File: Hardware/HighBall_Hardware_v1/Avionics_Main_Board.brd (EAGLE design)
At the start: 171.4 x 88.9 mm, 21 parts

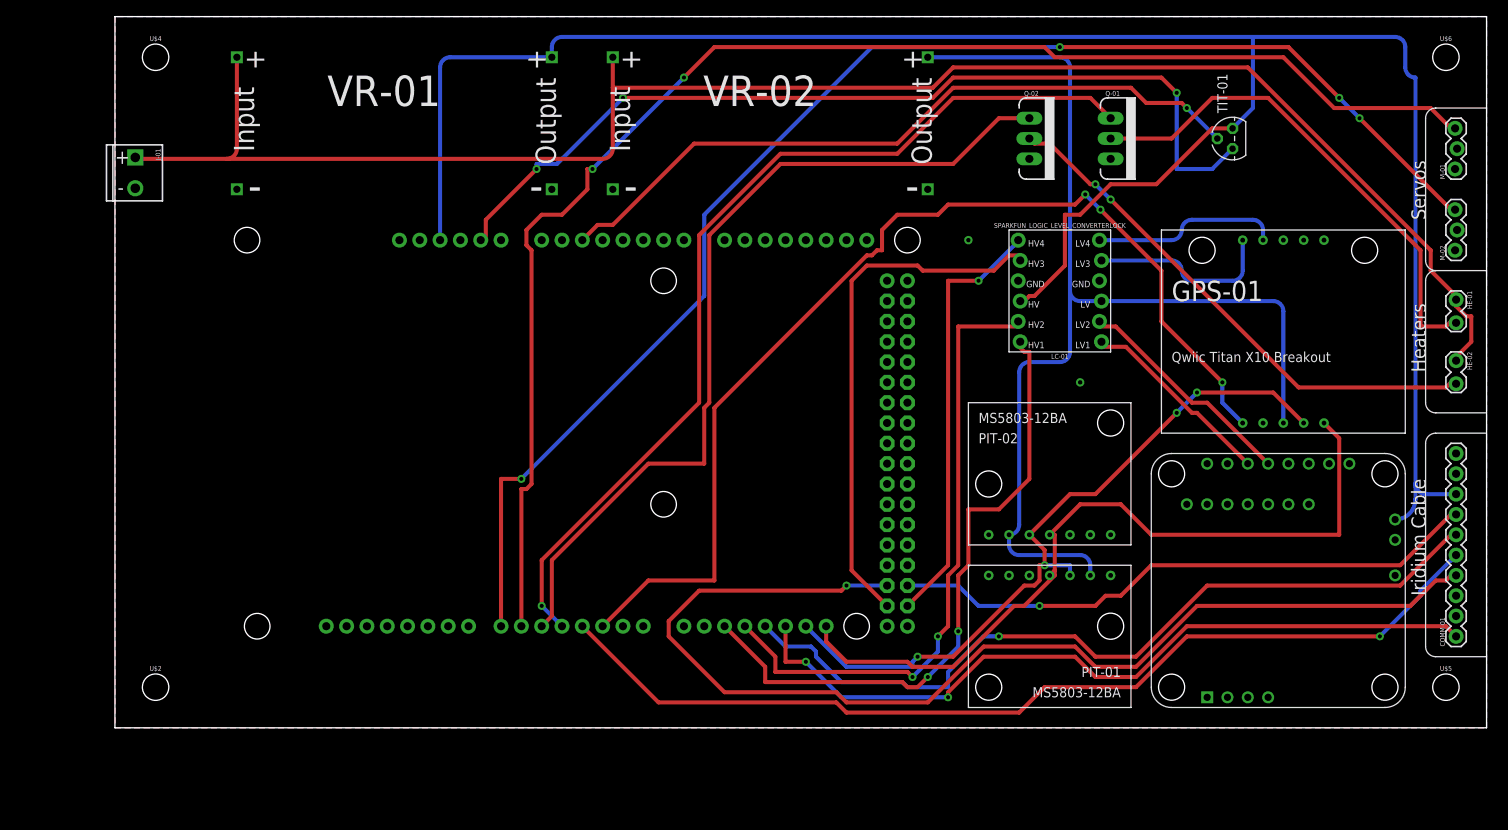
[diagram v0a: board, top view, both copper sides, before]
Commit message: Code and Schematic Updates
Added State Machine .h & .cpp file
Added Resistor to LM335 and added battery voltage measurement to schematic.
Board Layout TBD
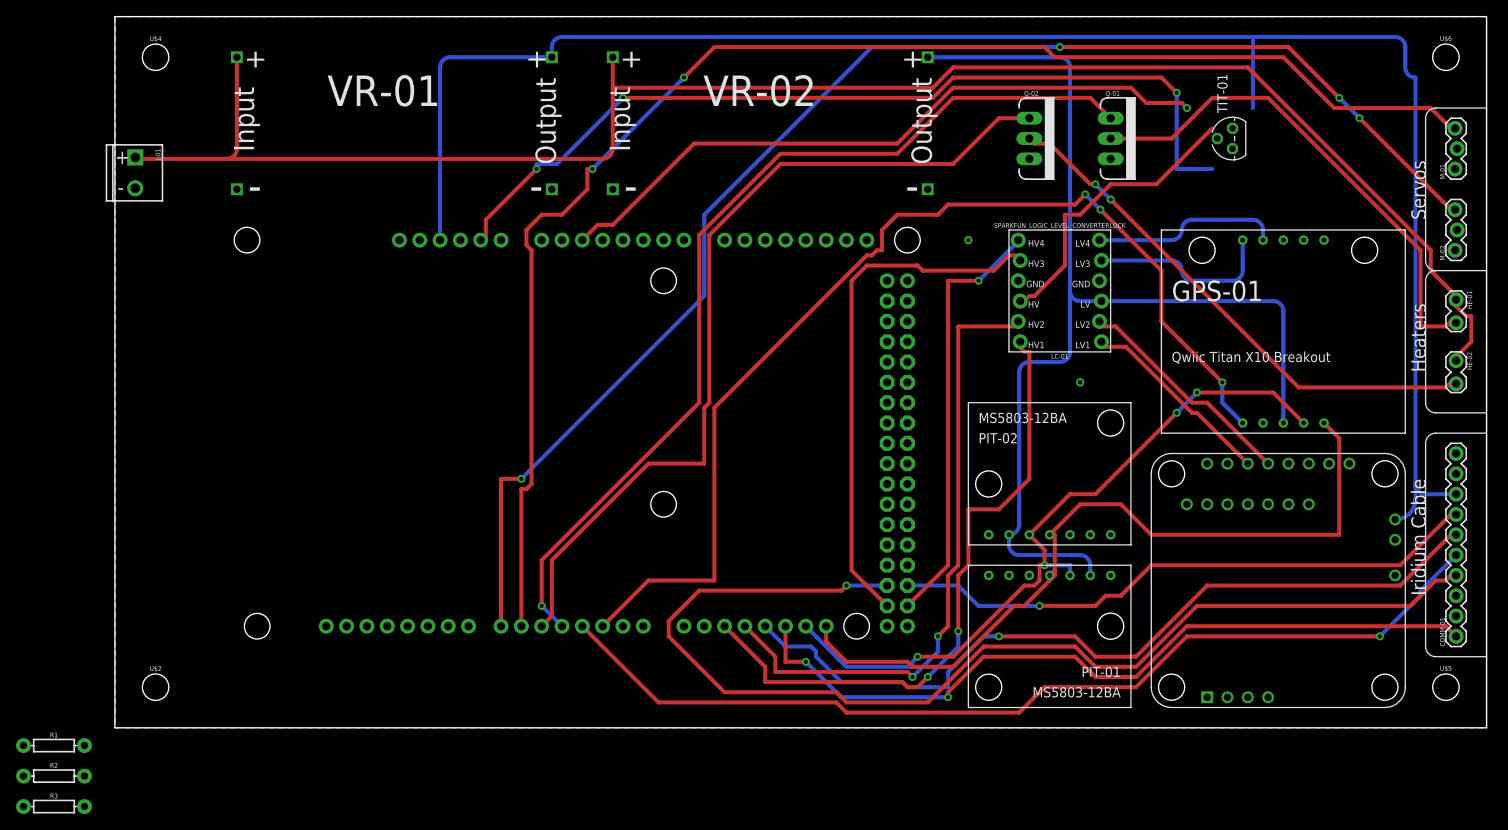
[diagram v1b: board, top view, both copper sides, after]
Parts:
- added R1: 2k, SparkFun-Resistors:AXIAL-0.3
- added R2: 20k, SparkFun-Resistors:AXIAL-0.3
- added R3: 130k, SparkFun-Resistors:AXIAL-0.3
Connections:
- new net VBAT_SENSE: C-1.A3, R2.P$1, R3.P$2
- net AGND: now also TIT-01.1; no longer TIT-01.3
- net GND: now also R3.P$1
- net TIT-01: now also R1.P$2
- net VBAT: now also R2.P$2
- net VCC_1: now also R1.P$1; no longer TIT-01.1
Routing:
- net VCC_1: track 263.0 -> 256.9 mm
- net TIT-01: track 89.9 -> 84.5 mm
- net AGND: track 115.6 -> 112.0 mm
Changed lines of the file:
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@@
 <?xml version="1.0" encoding="utf-8"?>
 <!DOCTYPE eagle SYSTEM "eagle.dtd">
-<eagle version="9.1.1">
+<eagle version="9.1.2">
 <drawing>
 <settings>
-<setting alwaysvectorfont="yes"/>
+<setting alwaysvectorfont="no"/>
 <setting verticaltext="up"/>
 </settings>
@@
 <element name="U$5" library="SparkFun-Hardware" library_urn="urn:adsk.eagle:library:519" package="STAND-OFF" package3d_urn="urn:adsk.eagle:package:38630/1" value="" x="166.37" y="5.08"/>
 <element name="U$6" library="SparkFun-Hardware" library_urn="urn:adsk.eagle:library:519" package="STAND-OFF" package3d_urn="urn:adsk.eagle:package:38630/1" value="" x="166.37" y="83.82"/>
+<element name="R1" library="SparkFun-Resistors" library_urn="urn:adsk.eagle:library:532" package="AXIAL-0.3" package3d_urn="urn:adsk.eagle:package:39658/1" value="2k" x="-7.62" y="-2.2225">
+<attribute name="PROD_ID" value="RES-08380" x="-7.62" y="-2.2225" size="1.778" layer="27" display="off"/>
+</element>
+<element name="R2" library="SparkFun-Resistors" library_urn="urn:adsk.eagle:library:532" package="AXIAL-0.3" package3d_urn="urn:adsk.eagle:package:39658/1" value="20k" x="-7.62" y="-6.0325">
+<attribute name="PROD_ID" value="RES-08380" x="-7.62" y="-6.0325" size="1.778" layer="27" display="off"/>
+</element>
+<element name="R3" library="SparkFun-Resistors" library_urn="urn:adsk.eagle:library:532" package="AXIAL-0.3" package3d_urn="urn:adsk.eagle:package:39658/1" value="130k" x="-7.62" y="-9.8425">
+<attribute name="PROD_ID" value="RES-08380" x="-7.62" y="-9.8425" size="1.778" layer="27" display="off"/>
+</element>
 </elements>
 <signals>
@@
 <wire x1="62.23" y1="80.01" x2="102.235" y2="80.01" width="0.508" layer="1"/>
 <wire x1="167.64" y1="53.975" x2="167.64" y2="53.5178" width="0.508" layer="1"/>
+<contactref element="R2" pad="P$2"/>
+<wire x1="-3.81" y1="-6.0325" x2="2.7178" y2="71.12" width="0" layer="19" extent="1-1"/>
 </signal>
 <signal name="GND">
@@
 <via x="106.68" y="60.96" extent="1-16" drill="0.55"/>
 <via x="120.65" y="43.18" extent="1-16" drill="0.55"/>
+<contactref element="R3" pad="P$1"/>
+<wire x1="160.02" y1="23.495" x2="167.64" y2="34.29" width="0" layer="19" extent="1-1"/>
+<wire x1="143.51" y1="38.1" x2="160.02" y2="23.495" width="0" layer="19" extent="1-1"/>
+<wire x1="120.65" y1="43.18" x2="143.51" y2="38.1" width="0" layer="19" extent="1-1"/>
+<wire x1="123.063" y1="55.88" x2="120.65" y2="43.18" width="0" layer="19" extent="1-1"/>
+<wire x1="112.903" y1="55.88" x2="123.063" y2="55.88" width="0" layer="19" extent="1-1"/>
+<wire x1="106.68" y1="60.96" x2="112.903" y2="55.88" width="0" layer="19" extent="1-1"/>
+<wire x1="101.6" y1="67.31" x2="106.68" y2="60.96" width="0" layer="19" extent="1-1"/>
+<wire x1="114.3" y1="71.12" x2="106.68" y2="60.96" width="0" layer="19" extent="1-1"/>
+<wire x1="124.46" y1="71.12" x2="114.3" y2="71.12" width="0" layer="19" extent="1-1"/>
+<wire x1="109.22" y1="24.13" x2="120.65" y2="43.18" width="0" layer="19" extent="1-1"/>
+<wire x1="124.46" y1="19.05" x2="109.22" y2="24.13" width="0" layer="19" extent="1-1"/>
+<wire x1="62.23" y1="67.31" x2="101.6" y2="67.31" width="0" layer="19" extent="1-1"/>
+<wire x1="54.61" y1="67.31" x2="62.23" y2="67.31" width="0" layer="19" extent="1-1"/>
+<wire x1="43.18" y1="60.96" x2="54.61" y2="67.31" width="0" layer="19" extent="1-1"/>
+<wire x1="15.24" y1="67.31" x2="43.18" y2="60.96" width="0" layer="19" extent="1-1"/>
+<wire x1="2.54" y1="67.4422" x2="15.24" y2="67.31" width="0" layer="19" extent="1-1"/>
+<wire x1="-11.43" y1="-9.8425" x2="2.54" y2="67.4422" width="0" layer="19" extent="1-1"/>
 </signal>
 <signal name="VCC_1">
 <contactref element="VR-01" pad="OUT+"/>
 <contactref element="C-1" pad="5V@0"/>
-<contactref element="TIT-01" pad="1"/>
 <contactref element="IMU-01" pad="VBAT"/>
 <contactref element="LC-01" pad="HV"/>
@@
 <wire x1="160.02" y1="86.36" x2="142.24" y2="86.36" width="0.508" layer="16"/>
 <wire x1="142.24" y1="86.36" x2="55.88" y2="86.36" width="0.508" layer="16"/>
-<wire x1="142.24" y1="77.47" x2="139.7" y2="74.93" width="0.508" layer="16"/>
 <wire x1="142.24" y1="86.36" x2="142.24" y2="77.47" width="0.508" layer="16"/>
 <wire x1="114.3" y1="53.975" x2="113.665" y2="53.34" width="0.508" layer="1"/>
@@
 <wire x1="130.175" y1="67.945" x2="124.46" y2="67.945" width="0.508" layer="1"/>
 <wire x1="137.16" y1="74.93" x2="130.175" y2="67.945" width="0.508" layer="1"/>
-<wire x1="139.7" y1="74.93" x2="137.16" y2="74.93" width="0.508" layer="1"/>
 <wire x1="113.665" y1="53.34" x2="113.157" y2="53.34" width="0.508" layer="1"/>
+<contactref element="R1" pad="P$1"/>
+<wire x1="142.24" y1="77.47" x2="137.16" y2="74.93" width="0" layer="19" extent="1-16"/>
+<wire x1="-11.43" y1="-2.2225" x2="40.64" y2="60.96" width="0" layer="19" extent="1-1"/>
 </signal>
 <signal name="VCC_2">
@@
 <signal name="AGND">
 <contactref element="C-1" pad="GND@1"/>
-<contactref element="TIT-01" pad="3"/>
-<wire x1="137.16" y1="69.85" x2="139.7" y2="72.39" width="0.508" layer="16"/>
 <wire x1="132.715" y1="69.85" x2="137.16" y2="69.85" width="0.508" layer="16"/>
 <wire x1="132.715" y1="79.375" x2="132.715" y2="69.85" width="0.508" layer="16"/>
@@
 <via x="63.5" y="78.74" extent="1-16" drill="0.508"/>
 <via x="52.705" y="69.85" extent="1-16" drill="0.508"/>
+<contactref element="TIT-01" pad="1"/>
+<wire x1="137.16" y1="69.85" x2="139.7" y2="74.93" width="0" layer="19" extent="16-16"/>
 </signal>
 <signal name="TIT-01">
 <contactref element="C-1" pad="A2"/>
-<contactref element="TIT-01" pad="2"/>
-<wire x1="133.985" y1="77.47" x2="137.795" y2="73.66" width="0.508" layer="16"/>
 <wire x1="133.35" y1="78.105" x2="133.985" y2="77.47" width="0.508" layer="1"/>
 <wire x1="128.905" y1="78.105" x2="133.35" y2="78.105" width="0.508" layer="1"/>
@@
 <wire x1="58.42" y1="60.96" x2="60.325" y2="62.865" width="0.508" layer="1"/>
 <via x="133.985" y="77.47" extent="1-16" drill="0.508"/>
+<contactref element="R1" pad="P$2"/>
+<contactref element="TIT-01" pad="2"/>
+<wire x1="133.985" y1="77.47" x2="137.795" y2="73.66" width="0" layer="19" extent="1-1"/>
+<wire x1="-3.81" y1="-2.2225" x2="58.42" y2="60.96" width="0" layer="19" extent="1-1"/>
 </signal>
 <signal name="IMU-01-RX">
@@
 <via x="115.57" y="15.24" extent="1-16" drill="0.508"/>
 </signal>
+<signal name="VBAT_SENSE">
+<contactref element="R2" pad="P$1"/>
+<contactref element="R3" pad="P$2"/>
+<contactref element="C-1" pad="A3"/>
+<wire x1="-3.81" y1="-9.8425" x2="60.96" y2="60.96" width="0" layer="19" extent="1-1"/>
+<wire x1="-11.43" y1="-6.0325" x2="-3.81" y2="-9.8425" width="0" layer="19" extent="1-1"/>
+</signal>
 </signals>

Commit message: Schematic Rev C and CAD Files changes
Completed rev C of hardware schematic
Created new PCB layout
Updated tolerance on ballast dispenser
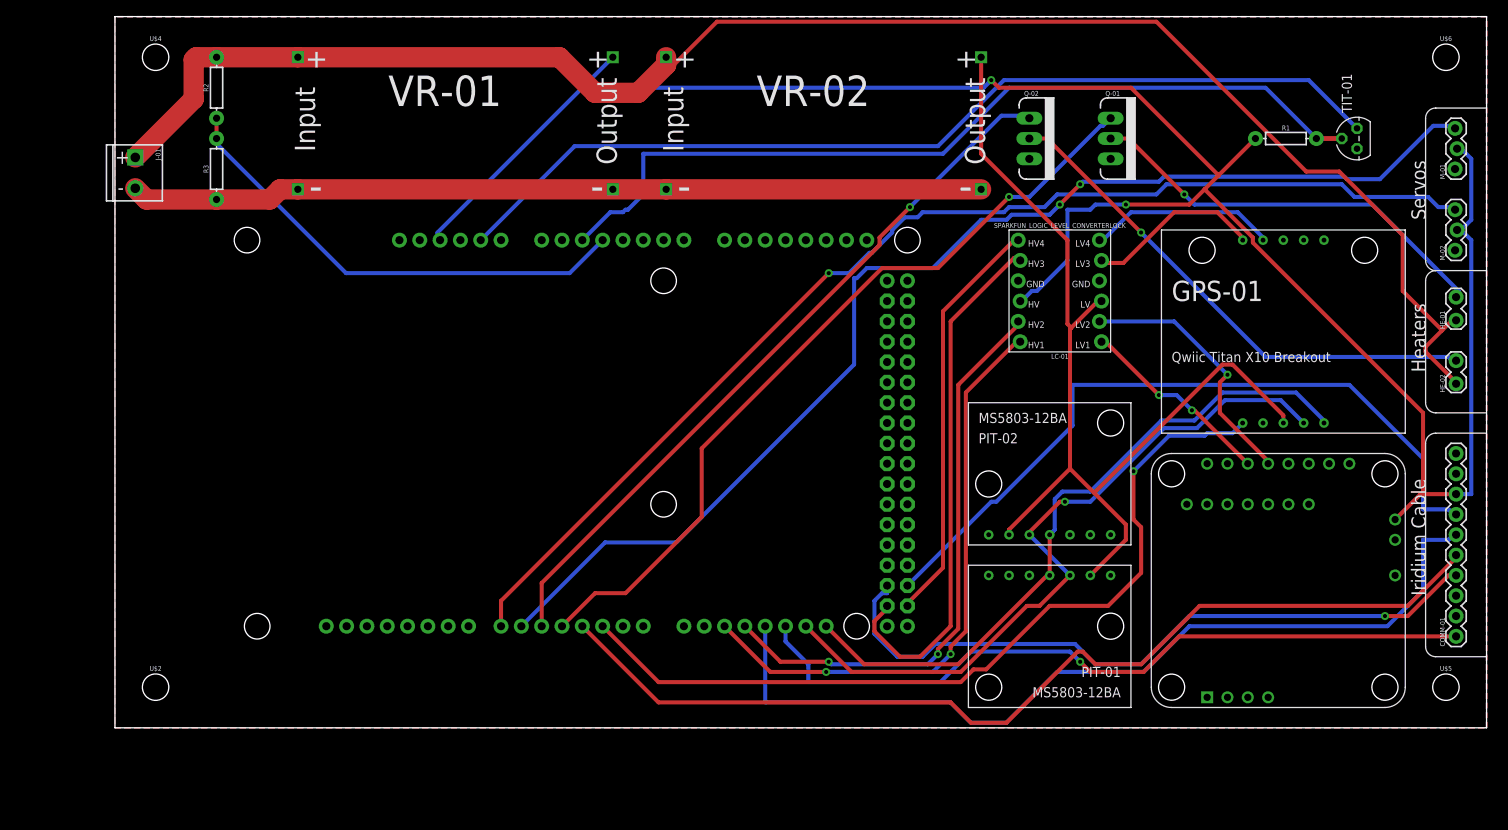
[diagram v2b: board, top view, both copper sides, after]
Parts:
- moved R1 171.7 mm to (146.4, 73.7)
- moved R2 88.4 mm to (12.7, 80.0), turned to 90 degrees
- moved R3 82.2 mm to (12.7, 69.8), turned to 90 degrees
- moved TIT-01 15.6 mm to (155.3, 73.7)
- moved VR-01 7.62 mm to (22.9, 67.3)
- moved VR-02 6.67 mm to (68.9, 67.3)
- moved HE-02 2.54 mm to (167.6, 43.2), turned to 90 degrees
- moved HE-01 2.22 mm to (167.6, 51.1), turned to 90 degrees
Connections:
- removed net N$3: M-01.1
- removed net N$4: M-01.2
- removed net N$6: M-02.2
- removed net N$7: M-02.1
- net GND: now also M-01.1, M-02.1
- net VCC_1: now also M-01.2, M-02.2
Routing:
- net GND: track 0.00 -> 106.8 mm, vias 2 -> 0
- net VBAT_SENSE: track 0.00 -> 59.9 mm
- net COMM-01-NETAV: track 141.6 -> 87.3 mm
- net M-01: track 181.9 -> 149.3 mm
- net M-02: track 174.4 -> 145.5 mm, vias 4 -> 1
- net GPS-01-INT: track 133.5 -> 105.1 mm, vias 3 -> 1
- net TIT-01: track 84.5 -> 108.4 mm, vias 1 -> 0
- net HE-01: track 118.1 -> 99.9 mm
- net COMM-01-ON/OFF: track 74.4 -> 92.4 mm, vias 1 -> 0
- net HE-02: track 107.7 -> 91.2 mm, vias 0 -> 1
- net VCC_2: track 137.6 -> 124.7 mm
- net SCL: track 97.3 -> 85.6 mm
- net N$1: track 63.1 -> 52.5 mm, vias 0 -> 1
- net COMM-01-TXD: track 101.0 -> 110.4 mm, vias 1 -> 0
- net AGND: track 112.0 -> 120.3 mm, vias 3 -> 0
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
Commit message: Electrical board changes
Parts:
- added COMM-02: (no value), SparkFun-Connectors:1X03_LOCK
- R2: value 20k -> 18k
- R3: value 130k -> 150k
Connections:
- net N$1 renamed HE-01_OUT
- net N$2 renamed HE-02_OUT
- new net COMM-02-RX: C-1.1, COMM-02.1
- new net COMM-02-TX: C-1.0, COMM-02.2
- net GND: now also COMM-02.3
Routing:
- net GND: track 106.8 -> 21.0 mm, vias 0 -> 6
- net TIT-01: track 108.4 -> 182.4 mm, vias 0 -> 3
- net COMM-01-NETAV: track 87.3 -> 153.7 mm, vias 1 -> 0
- net AGND: track 120.3 -> 183.1 mm, vias 0 -> 2
- net GPS-01-INT: track 105.1 -> 146.1 mm, vias 1 -> 2
- net IMU-01-RX_HV: track 74.5 -> 114.1 mm
- net IMU-01-TX_HV: track 72.5 -> 107.9 mm
- net HE-01: track 99.9 -> 131.8 mm, vias 1 -> 4
- net M-02: track 145.5 -> 175.0 mm, vias 1 -> 4
- net HE-02: track 91.2 -> 119.6 mm, vias 1 -> 0
- net M-01: track 149.3 -> 174.5 mm, vias 2 -> 6
- net COMM-01-RI: track 124.4 -> 145.0 mm
- net VBAT: track 209.4 -> 227.5 mm
- net VCC_1: track 264.2 -> 281.5 mm, vias 2 -> 5
- net COMM-02-RX: track 0.00 -> 11.0 mm, vias 0 -> 2
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
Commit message: Electronics and Hardware changes
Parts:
- removed R1: 2k, SparkFun-Resistors:AXIAL-0.3
- COMM-02: device SparkFun-Connectors:1X03_LOCK -> SparkFun-Connectors:1X05_LOCK
- R3: value 150k -> 15k
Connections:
- net COMM-02-RX renamed COMM-02-TXO
- net COMM-02-TX renamed COMM-02-RXI
- new net 5V: TIT-01.3
- net GND: now also COMM-02.5; no longer COMM-02.3
- net TIT-01: no longer R1.P$2
- net VCC_1: no longer R1.P$1
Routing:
- net COMM-01-RI: track 145.0 -> 156.1 mm
- net TIT-01: track 182.4 -> 179.2 mm, vias 3 -> 4
- net GND: track 21.0 -> 23.2 mm, vias 6 -> 9
- net COMM-01-NETAV: track 153.7 -> 152.1 mm, vias 0 -> 2
- net VBAT: track 227.5 -> 228.7 mm
- net VCC_1: track 281.5 -> 280.3 mm, vias 5 -> 7
- net M-01: track 174.5 -> 175.1 mm
- net VCC_2: track 126.1 -> 126.5 mm, vias 1 -> 2
- net SCL: track 84.2 -> 84.1 mm, vias 1 -> 2
- net SDA: track 97.9 -> 98.0 mm, vias 3 -> 4
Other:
- board size 171.4 x 88.9 mm -> 172.1 x 88.9 mm

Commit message: Added ground for IMU
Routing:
- net GND: track 23.2 -> 26.3 mm, vias 9 -> 10
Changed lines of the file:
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@@
 <wire x1="167.513" y1="59.69" x2="168.783" y2="58.42" width="0.635" layer="16"/>
 <wire x1="168.783" y1="58.42" x2="168.91" y2="58.42" width="0.635" layer="16"/>
+<wire x1="160.02" y1="23.495" x2="160.7257" y2="24.2007" width="0.635" layer="16"/>
+<wire x1="160.7257" y1="24.2007" x2="160.77979375" y2="24.2007" width="0.635" layer="16"/>
+<wire x1="160.77979375" y1="24.2007" x2="161.8543" y2="25.27520625" width="0.635" layer="16"/>
+<wire x1="161.8543" y1="25.27520625" x2="161.8543" y2="25.3293" width="0.635" layer="16"/>
+<wire x1="161.8543" y1="25.3293" x2="161.925" y2="25.4" width="0.635" layer="16"/>
+<wire x1="161.925" y1="25.4" x2="162.24038125" y2="25.4" width="0.635" layer="16"/>
+<via x="162.24038125" y="25.4" extent="1-16" drill="0.899159375"/>
 </signal>
 <signal name="VCC_1" class="1">
